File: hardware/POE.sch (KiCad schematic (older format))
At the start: 122 parts, among them J1 0813-1X1T-57-F, J2 SWD, J3 MCU Port B, J4 MCU Port C, P1 PoE-, P2 PoE+, P3 GND, P4 +5V, P5 +12V, P6 +3V3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

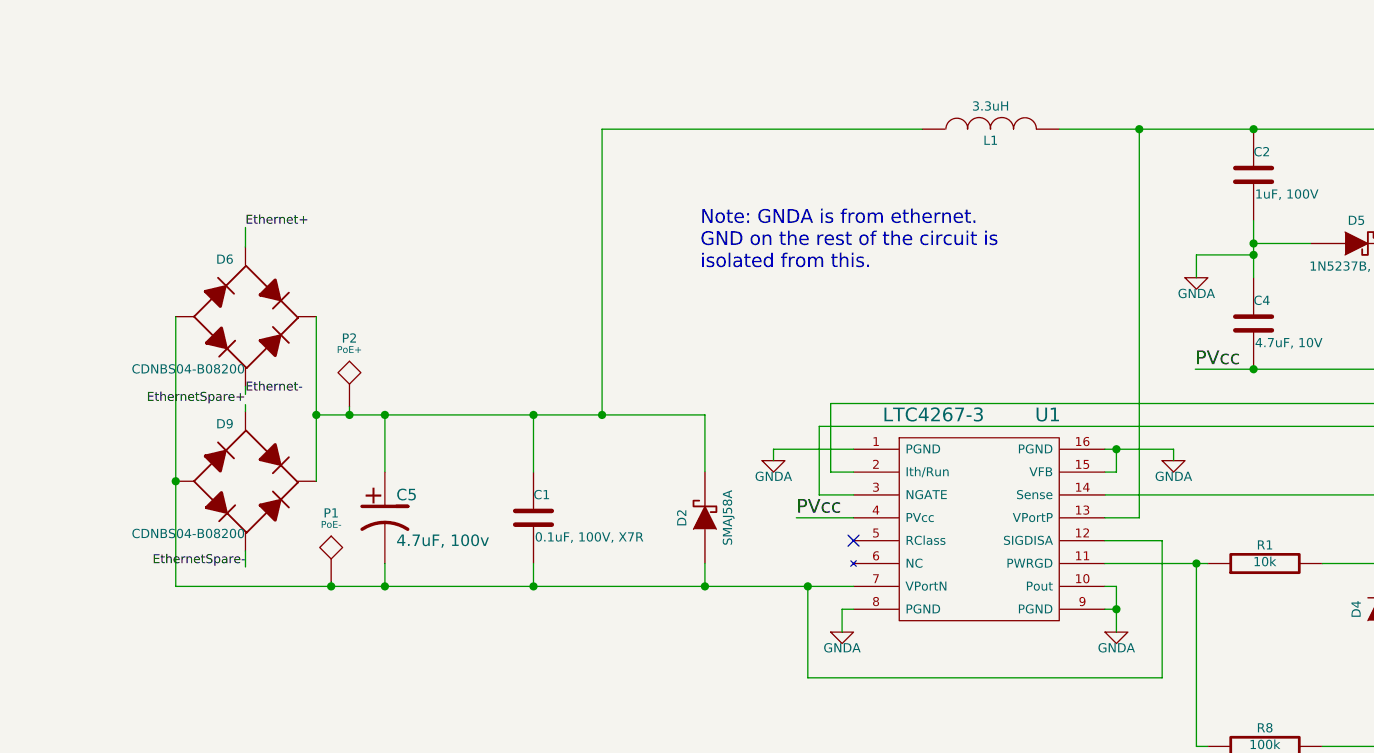
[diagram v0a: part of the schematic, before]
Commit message: Changed C5 to connect it to GNDA instead of VPortN. See http://jonneal.me/error-in-linear-tech-design-note-361/ for reason why.
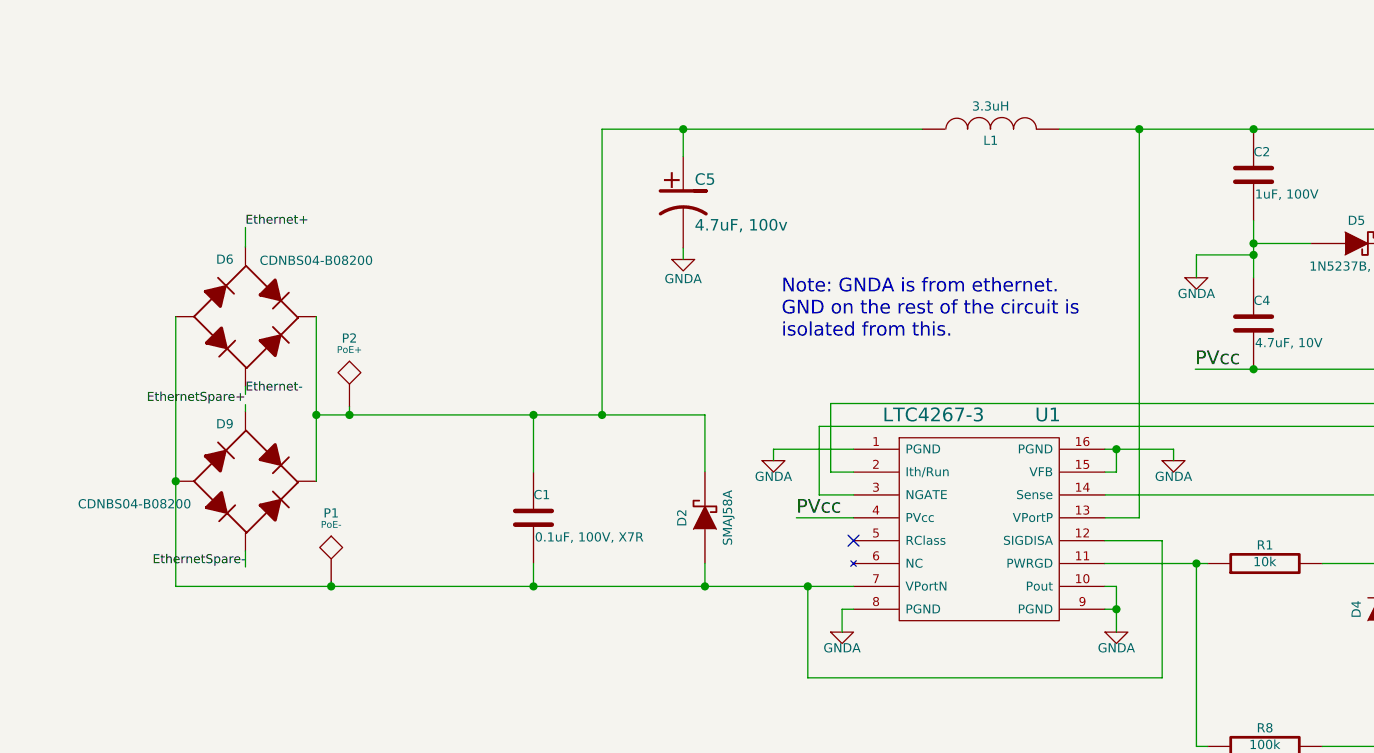
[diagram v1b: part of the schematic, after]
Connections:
- net GNDA: now also C5.2
- net at C1.2, D2.1 (A), D6.4 (-)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: no longer C5.2
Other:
- moved on the sheet: C5
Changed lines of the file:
@@
 LIBS:valves
 LIBS:rfid
-LIBS:rfidAndPOE-cache
+LIBS:POE-cache
 EELAYER 24 0
 EELAYER END
@@
 L CP1 C5
 U 1 1 529972BA
-P 2355 2715
-F 0 "C5" H 2405 2815 50  0000 L CNN
-F 1 "4.7uF, 100v" H 2405 2615 50  0000 L CNN
-F 2 "rfid:EEE-2AA4R7UP" H 2355 2715 60  0001 C CNN
-F 3 "" H 2355 2715 60  0000 C CNN
-	1    2355 2715
+P 3660 1335
+F 0 "C5" H 3710 1435 50  0000 L CNN
+F 1 "4.7uF, 100v" H 3710 1235 50  0000 L CNN
+F 2 "rfid:EEE-2AA4R7UP" H 3660 1335 60  0001 C CNN
+F 3 "" H 3660 1335 60  0000 C CNN
+	1    3660 1335
 	1    0    0    -1
 $EndComp
@@
 	1    0    0    -1
 $EndComp
-Text Notes 3735 1635 0    60   ~ 0
+Text Notes 4090 1935 0    60   ~ 0
 Note: GNDA is from ethernet. \nGND on the rest of the circuit is\nisolated from this.
 $Comp
@@
 P 1745 2555
 F 0 "D9" H 1655 2805 40  0000 C CNN
-F 1 "CDNBS04-B08200" H 1495 2325 40  0000 C CNN
+F 1 "CDNBS04-B08200" H 1260 2455 40  0000 C CNN
 F 2 "rfid:CDNBS04" H 1520 2765 60  0001 C CNN
 F 3 "" H 1520 2765 60  0000 C CNN
@@
 P 1745 1835
 F 0 "D6" H 1655 2085 40  0000 C CNN
-F 1 "CDNBS04-B08200" H 1495 1605 40  0000 C CNN
+F 1 "CDNBS04-B08200" H 2055 2080 40  0000 C CNN
 F 2 "rfid:CDNBS04" H 1520 2045 60  0001 C CNN
 F 3 "" H 1520 2045 60  0000 C CNN
@@
 Wire Wire Line
 	1440 3015 4405 3015
-Connection ~ 2355 2265
 Connection ~ 3005 2265
 Wire Wire Line
@@
 	2055 2265 3755 2265
 Wire Wire Line
-	2355 2915 2355 3015
-Connection ~ 2355 3015
-Wire Wire Line
 	3005 2915 3005 3015
 Wire Wire Line
@@
 Wire Wire Line
 	3005 2515 3005 2265
-Wire Wire Line
-	2355 2515 2355 2265
 Connection ~ 3305 2265
 Wire Wire Line
@@
 	9315 2065 9315 1990
 Connection ~ 9315 1990
+$Comp
+L GNDA #PWR?
+U 1 1 54332B1C
+P 3660 1585
+F 0 "#PWR?" H 3660 1585 40  0001 C CNN
+F 1 "GNDA" H 3660 1500 40  0000 C CNN
+F 2 "" H 3660 1585 60  0000 C CNN
+F 3 "" H 3660 1585 60  0000 C CNN
+	1    3660 1585
+	1    0    0    -1
+$EndComp
+Wire Wire Line
+	3660 1135 3660 1015
+Connection ~ 3660 1015
+Wire Wire Line
+	3660 1535 3660 1585
 $EndSCHEMATC
